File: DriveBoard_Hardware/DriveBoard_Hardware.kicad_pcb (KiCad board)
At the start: 2 copper layers, 20 parts, among them U1 MAX_3232, U2 MAX_3232, U3 OKI, U4 TM4C129E_Launchpad

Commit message: Made pcb layout
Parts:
- moved U1 93.7 mm to (136.1, 78.5)
- moved C7 91.1 mm to (161.7, 81.5)
- moved Conn2 88.0 mm to (131.3, 49.0)
- moved C3 87.9 mm to (129.7, 73.7)
- moved C4 84.3 mm to (129.7, 79.0)
- moved C8 81.7 mm to (161.7, 90.4)
- moved C9 80.9 mm to (145.8, 88.1)
- moved C11 80.6 mm to (158.9, 87.4)
- moved C2 80.0 mm to (126.1, 81.5)
- moved C1 77.9 mm to (126.1, 76.5)
- moved C12 76.7 mm to (142.4, 72.9)
- moved C10 74.7 mm to (145.9, 93.7)
- moved C5 73.4 mm to (142.2, 91.2)
- moved Conn3 70.5 mm to (148.6, 49.0)
- moved C6 68.0 mm to (142.1, 96.0)
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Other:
- board outline added: 61 x 99.8 mm

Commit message: Added PDR text files and made a few changes
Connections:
- net Net-(C7-Pad1) renamed /+12V
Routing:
- net +5V: track 0.00 -> 37.1 mm
- net /+12V: track 0.00 -> 26.6 mm

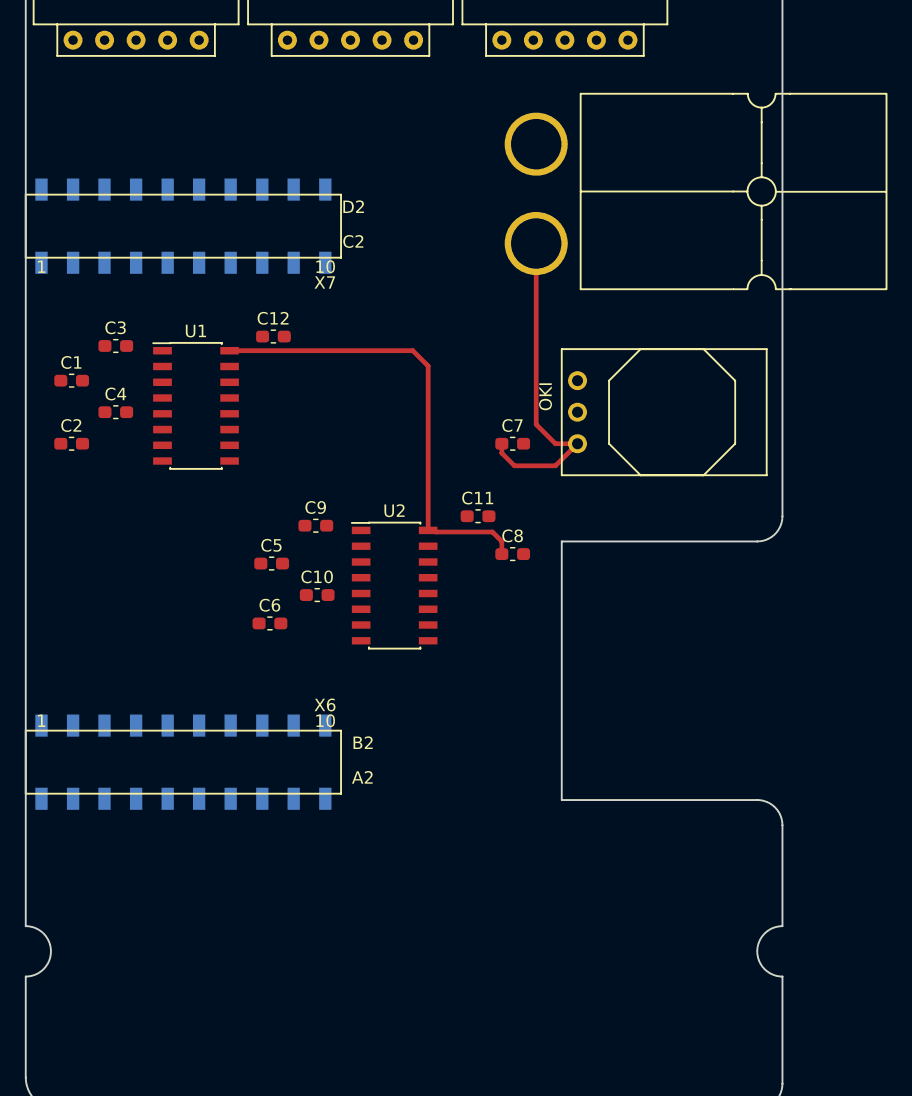
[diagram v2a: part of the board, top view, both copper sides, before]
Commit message: Updated silkscreens
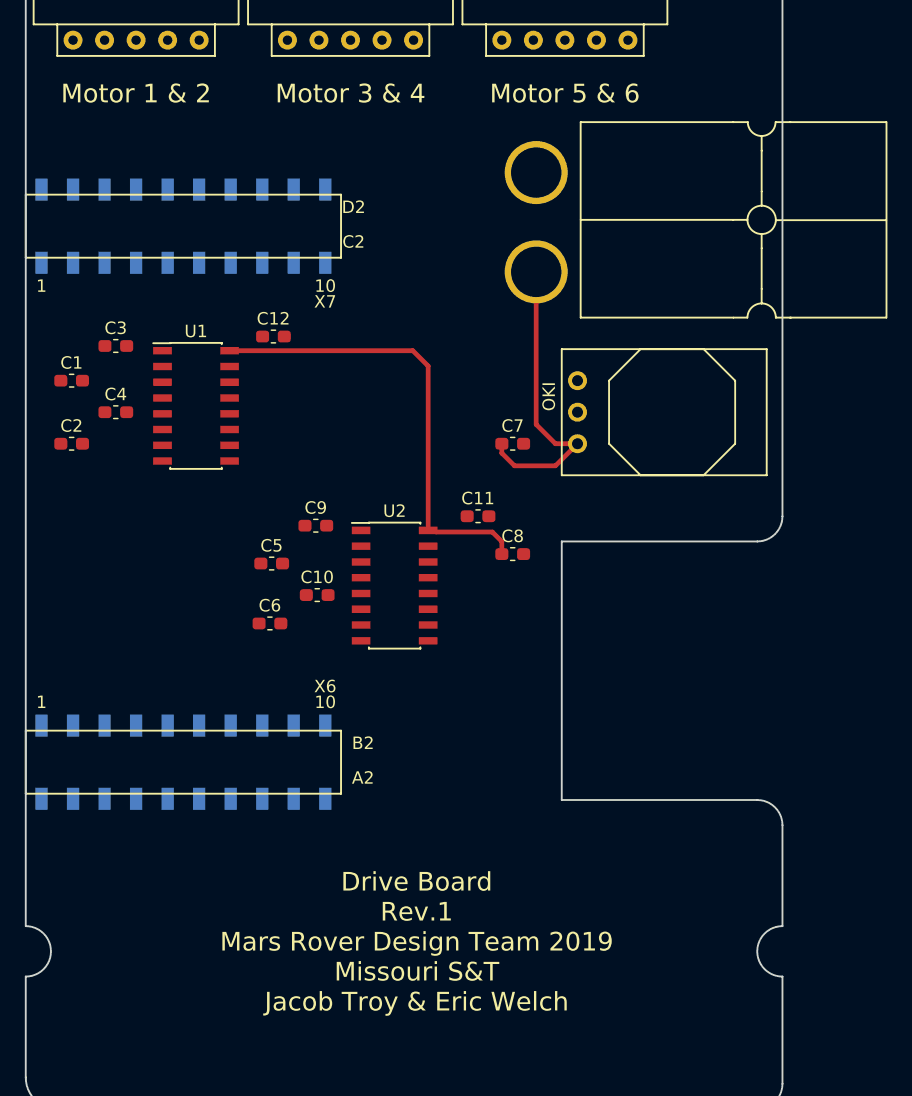
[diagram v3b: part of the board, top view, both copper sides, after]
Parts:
- moved Conn1 2.29 mm to (167.1, 55.6)
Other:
- board text added: "Drive Board Rev.1 Mars Rover Design Team 2019 Missouri S&T Jacob Troy & Eric Welch"
- board text added: "Motor 1 & 2"
- board text added: "Motor 3 & 4"
- board text added: "Motor 5 & 6"
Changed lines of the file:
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@@
   (general
     (thickness 1.6)
-    (drawings 17)
+    (drawings 21)
     (tracks 15)
     (zones 0)
@@
   )
   (module MRDT_Connectors:Anderson_2_Horisontal_Side_by_Side (layer F.Cu)
-    (at 167.132 53.34 180)
+    (at 167.132 55.626 180)
     (fp_text reference Conn1 (at -1.8796 0.762 180) (layer F.SilkS) hide
       (effects (font (size 1 1) (thickness 0.15)))
@@
       (effects (font (size 1 1) (thickness 0.15)))
     )
-    (fp_text value OKI (at 6.35 -1.27 90) (layer F.SilkS)
+    (fp_text value OKI (at 6.35 -1.016 90) (layer F.SilkS)
       (effects (font (size 1 1) (thickness 0.15)))
     )
@@
       (effects (font (size 1 1) (thickness 0.15)))
     )
-    (fp_text user 1 (at 1.27 -42.418 180) (layer F.SilkS)
-      (effects (font (size 1 1) (thickness 0.15)))
-    )
-    (fp_text user 10 (at 24.13 -42.418 180) (layer F.SilkS)
-      (effects (font (size 1 1) (thickness 0.15)))
-    )
-    (fp_text user 10 (at 24.13 -5.842 180) (layer F.SilkS)
-      (effects (font (size 1 1) (thickness 0.15)))
-    )
-    (fp_text user 1 (at 1.27 -5.842 180) (layer F.SilkS)
-      (effects (font (size 1 1) (thickness 0.15)))
-    )
-    (fp_text user X7 (at 24.13 -41.148 180) (layer F.SilkS)
-      (effects (font (size 1 1) (thickness 0.15)))
-    )
-    (fp_text user X6 (at 24.13 -7.112) (layer F.SilkS)
+    (fp_text user 1 (at 1.27 -40.894 180) (layer F.SilkS)
+      (effects (font (size 1 1) (thickness 0.15)))
+    )
+    (fp_text user 10 (at 24.13 -40.894 180) (layer F.SilkS)
+      (effects (font (size 1 1) (thickness 0.15)))
+    )
+    (fp_text user 10 (at 24.13 -7.366 180) (layer F.SilkS)
+      (effects (font (size 1 1) (thickness 0.15)))
+    )
+    (fp_text user 1 (at 1.27 -7.366 180) (layer F.SilkS)
+      (effects (font (size 1 1) (thickness 0.15)))
+    )
+    (fp_text user X7 (at 24.13 -39.624 180) (layer F.SilkS)
+      (effects (font (size 1 1) (thickness 0.15)))
+    )
+    (fp_text user X6 (at 24.13 -8.636) (layer F.SilkS)
       (effects (font (size 1 1) (thickness 0.15)))
     )
@@
       (net 67 "Net-(U4-PadPP5)"))
   )
+  (gr_text "Motor 5 & 6" (at 165.862 53.34) (layer F.SilkS)
+    (effects (font (size 1.5 1.5) (thickness 0.3)))
+  )
+  (gr_text "Motor 3 & 4" (at 148.59 53.34) (layer F.SilkS)
+    (effects (font (size 1.5 1.5) (thickness 0.3)))
+  )
+  (gr_text "Motor 1 & 2" (at 131.318 53.34) (layer F.SilkS)
+    (effects (font (size 1.5 1.5) (thickness 0.3)))
+  )
+  (gr_text "Drive Board\nRev.1\nMars Rover Design Team 2019\nMissouri S&T\nJacob Troy & Eric Welch" (at 153.924 121.666) (layer F.SilkS)
+    (effects (font (size 1.5 1.5) (thickness 0.3)))
+  )
   (gr_arc (start 181.356 87.376) (end 181.356 89.408) (angle -90) (layer Edge.Cuts) (width 0.15))

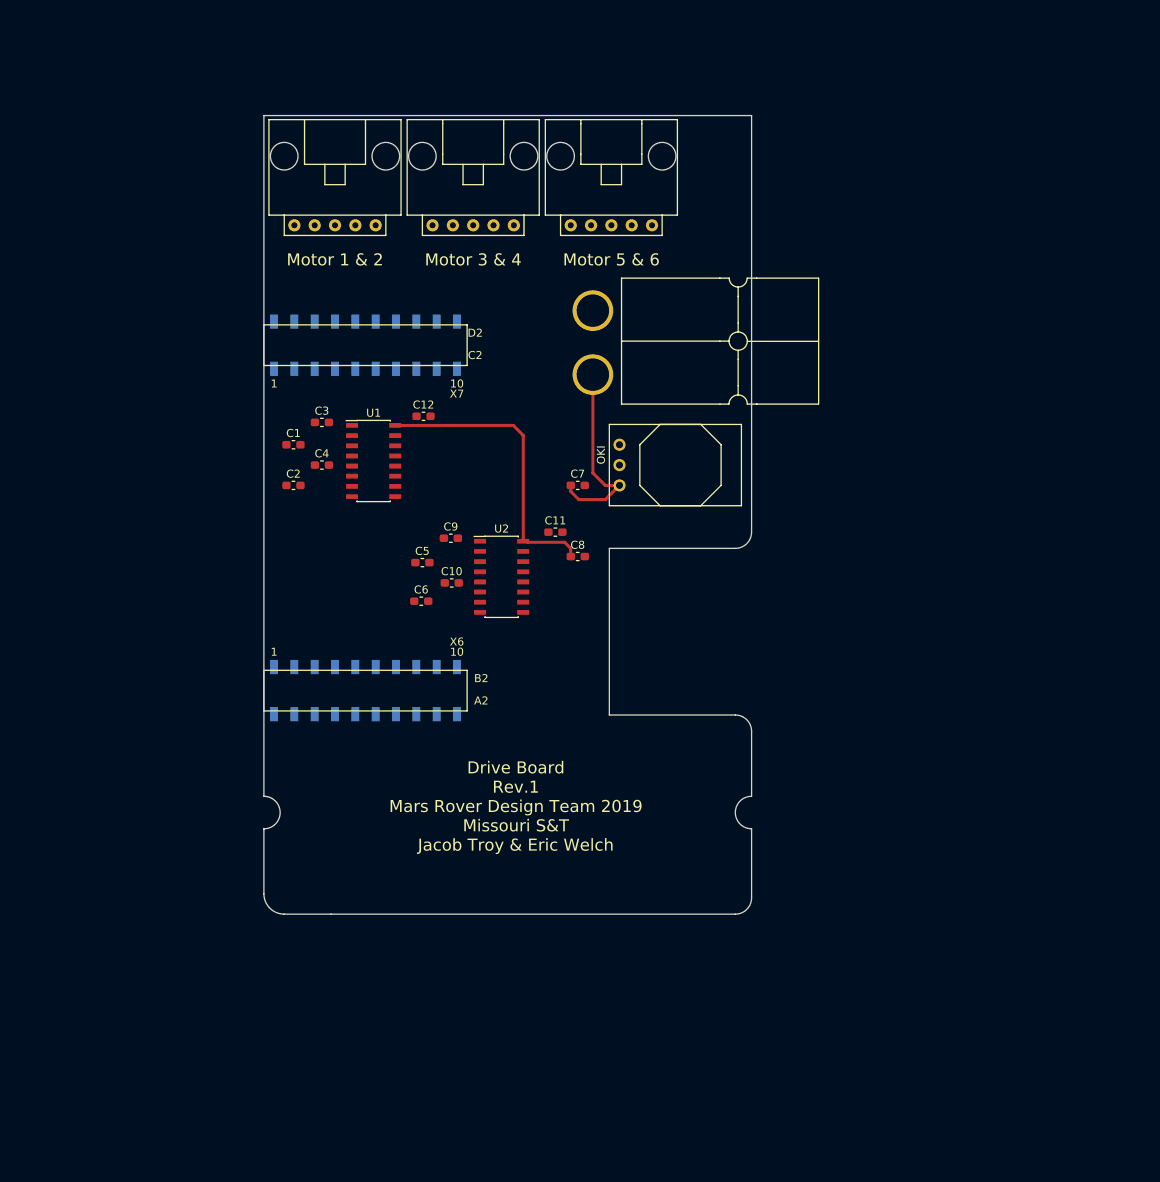
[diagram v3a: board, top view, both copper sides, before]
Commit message: Added traces to pcb layout
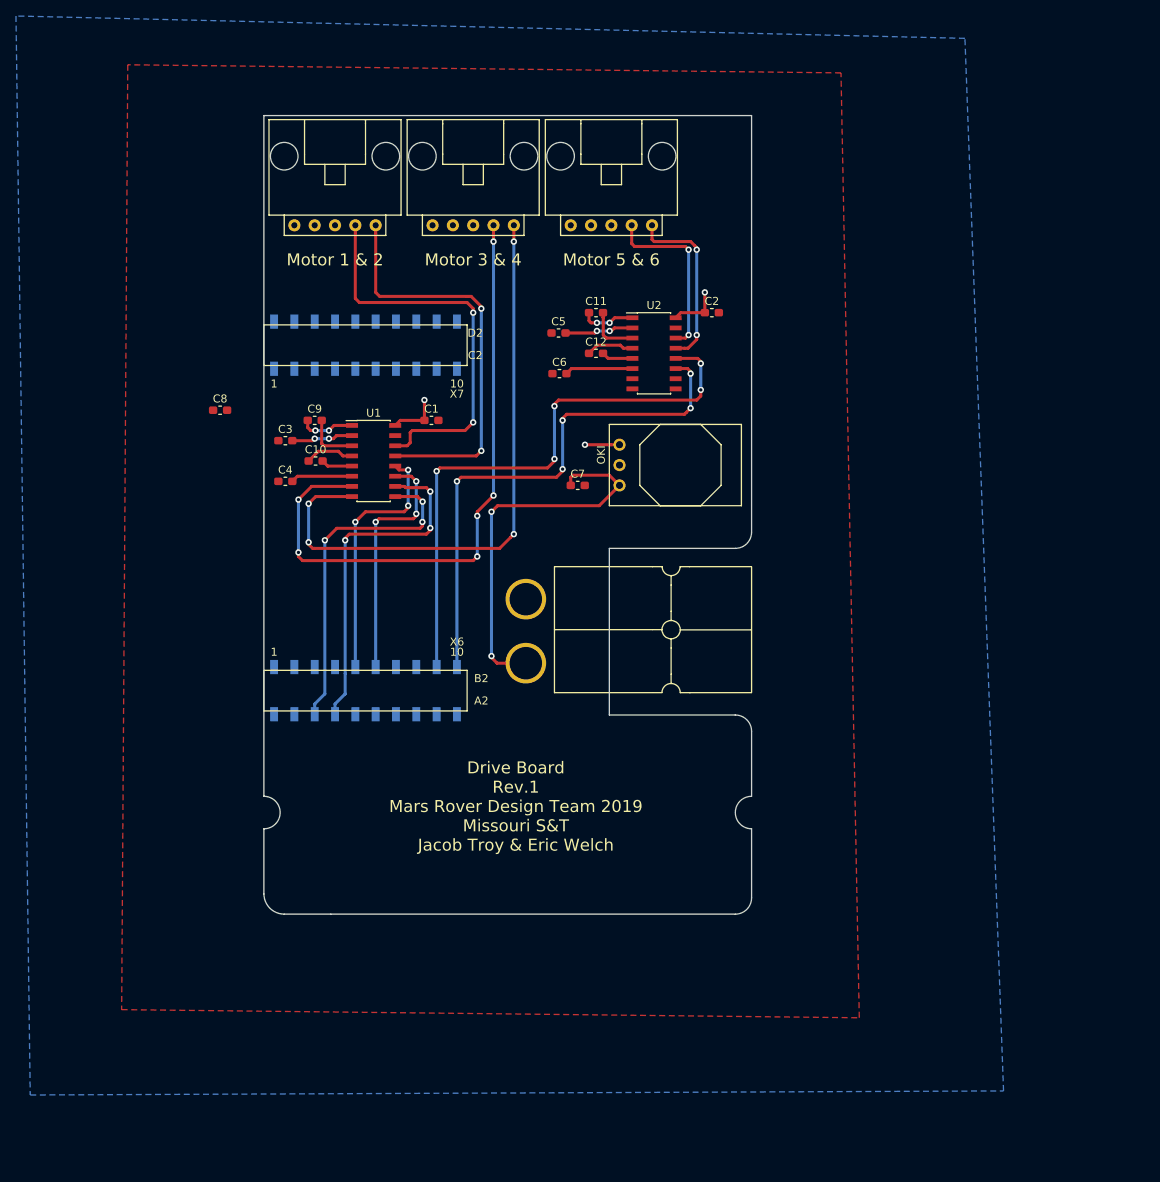
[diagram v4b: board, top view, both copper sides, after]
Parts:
- moved C2 56.6 mm to (178.4, 59.9)
- moved C8 48.3 mm to (117.0, 72.1)
- moved Conn1 37.0 mm to (158.8, 91.7)
- moved U2 33.8 mm to (171.2, 65.0)
- moved C5 33.4 mm to (159.3, 62.5)
- moved C6 33.3 mm to (159.4, 67.6)
- moved C11 27.9 mm to (163.9, 59.9)
- moved C12 23.0 mm to (163.9, 65.0)
- moved C10 22.8 mm to (128.9, 78.5)
- moved C9 22.5 mm to (128.8, 73.4)
- moved C1 17.5 mm to (143.4, 73.4)
- moved C3 5.11 mm to (125.1, 75.9)
- moved C4 5.00 mm to (125.1, 81.0)
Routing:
- net TX_2_SL: track 0.00 -> 79.5 mm, vias 0 -> 6
- net RX_2_SL: track 0.00 -> 76.1 mm, vias 0 -> 4
- net RX_3_IC: track 0.00 -> 73.2 mm, vias 0 -> 5
- net TX_3_IC: track 0.00 -> 66.7 mm, vias 0 -> 5
- net RX_1_SL: track 0.00 -> 51.4 mm, vias 0 -> 2
- net TX_1_SL: track 0.00 -> 50.3 mm, vias 0 -> 2
- net TX_2_IC: track 0.00 -> 43.1 mm, vias 0 -> 3
- net RX_2_IC: track 0.00 -> 41.9 mm, vias 0 -> 3
- net RX_1_IC: track 0.00 -> 32.0 mm, vias 0 -> 3
- net TX_1_IC: track 0.00 -> 30.7 mm, vias 0 -> 3
- net RX_3_SL: track 0.00 -> 22.4 mm, vias 0 -> 2
- net TX_3_SL: track 0.00 -> 22.2 mm, vias 0 -> 2
- net /+12V: track 26.6 -> 47.9 mm, vias 0 -> 2
- net +5V: track 37.1 -> 17.9 mm, vias 0 -> 3
- net Net-(C5-Pad2): track 0.00 -> 8.63 mm, vias 0 -> 2
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- added copper zone on B.Cu, net +5V
- added copper zone on F.Cu, net GND

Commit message: Updated some connections
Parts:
- moved C8 46.1 mm to (162.4, 80.0)
- moved C7 5.95 mm to (159.6, 87.1)
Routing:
- net +5V: track 17.9 -> 23.2 mm
- net /+12V: track 47.9 -> 43.2 mm
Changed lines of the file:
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@@
     (thickness 1.6)
     (drawings 21)
-    (tracks 260)
+    (tracks 264)
     (zones 0)
     (modules 20)
@@
   )
   (module Capacitor_SMD:C_0603_1608Metric_Pad1.05x0.95mm_HandSolder (layer F.Cu)
-    (at 161.657 81.534)
+    (at 159.625 87.122)
     (descr "Capacitor SMD 0603 (1608 Metric), square (rectangular) end terminal, IPC_7351 nominal with elongated pad for handsoldering. (Body size source: http://www.tortai-tech.com/upload/download/2011102023233369053.pdf), generated with kicad-footprint-generator")
     (tags "capacitor handsolder")
@@
   )
   (module Capacitor_SMD:C_0603_1608Metric_Pad1.05x0.95mm_HandSolder (layer F.Cu)
-    (at 116.953 72.136)
+    (at 162.419 80.01)
     (descr "Capacitor SMD 0603 (1608 Metric), square (rectangular) end terminal, IPC_7351 nominal with elongated pad for handsoldering. (Body size source: http://www.tortai-tech.com/upload/download/2011102023233369053.pdf), generated with kicad-footprint-generator")
     (tags "capacitor handsolder")
@@
   (segment (start 173.896 60.579) (end 174.346 60.579) (width 0.25) (layer F.Cu) (net 2))
   (via (at 162.56 76.454) (size 0.8) (drill 0.4) (layers F.Cu B.Cu) (net 2))
-  (segment (start 165.80037 76.454) (end 162.56 76.454) (width 0.381) (layer F.Cu) (net 2))
   (segment (start 166.878 76.454) (end 165.80037 76.454) (width 0.381) (layer F.Cu) (net 2))
   (segment (start 174.531 59.944) (end 173.896 60.579) (width 0.381) (layer F.Cu) (net 2))
@@
   (via (at 177.546 57.404) (size 0.8) (drill 0.4) (layers F.Cu B.Cu) (net 2))
   (segment (start 177.546 59.944) (end 177.546 57.404) (width 0.381) (layer F.Cu) (net 2))
+  (segment (start 163.83 76.454) (end 162.56 76.454) (width 0.381) (layer F.Cu) (net 2))
+  (segment (start 165.80037 76.454) (end 163.83 76.454) (width 0.381) (layer F.Cu) (net 2))
+  (segment (start 161.544 80.01) (end 161.544 78.994) (width 0.381) (layer F.Cu) (net 2))
+  (segment (start 161.544 78.994) (end 162.052 78.486) (width 0.381) (layer F.Cu) (net 2))
+  (segment (start 162.052 78.486) (end 163.576 78.486) (width 0.381) (layer F.Cu) (net 2))
+  (segment (start 163.83 78.232) (end 163.83 76.454) (width 0.381) (layer F.Cu) (net 2))
+  (segment (start 163.576 78.486) (end 163.83 78.232) (width 0.381) (layer F.Cu) (net 2))
   (via (at 128.778 75.692) (size 0.8) (drill 0.4) (layers F.Cu B.Cu) (net 3))
   (segment (start 125.984 75.946) (end 128.524 75.946) (width 0.381) (layer F.Cu) (net 3))
@@
   (segment (start 177.038 69.596) (end 177.038 70.358) (width 0.381) (layer F.Cu) (net 36))
   (segment (start 177.038 70.358) (end 176.53 70.866) (width 0.381) (layer F.Cu) (net 36))
-  (segment (start 165.608 80.264) (end 166.878 81.534) (width 0.381) (layer F.Cu) (net 68))
-  (segment (start 161.036 80.264) (end 165.608 80.264) (width 0.381) (layer F.Cu) (net 68))
-  (segment (start 160.782 81.534) (end 160.782 80.518) (width 0.381) (layer F.Cu) (net 68))
-  (segment (start 160.782 80.518) (end 161.036 80.264) (width 0.381) (layer F.Cu) (net 68))
   (segment (start 151.576498 103.758) (end 150.876 103.057502) (width 0.381) (layer F.Cu) (net 68))
   (segment (start 155.1686 103.758) (end 151.576498 103.758) (width 0.381) (layer F.Cu) (net 68))
@@
   (segment (start 164.338 84.074) (end 166.878 81.534) (width 0.381) (layer F.Cu) (net 68))
   (segment (start 150.876 84.836) (end 151.638 84.074) (width 0.381) (layer F.Cu) (net 68))
-  (segment (start 151.638 84.074) (end 164.338 84.074) (width 0.381) (layer F.Cu) (net 68))
+  (segment (start 158.75 84.074) (end 164.338 84.074) (width 0.381) (layer F.Cu) (net 68))
+  (segment (start 151.638 84.074) (end 158.75 84.074) (width 0.381) (layer F.Cu) (net 68))
+  (segment (start 158.75 87.122) (end 158.75 84.074) (width 0.381) (layer F.Cu) (net 68))
   (zone (net 1) (net_name GND) (layer F.Cu) (hatch edge 0.508)
-    (connect_pads (clearance 0.508))
+    (connect_pads yes (clearance 0.508))
     (min_thickness 0.254)
     (fill yes (arc_segments 16) (thermal_gap 0.508) (thermal_bridge_width 0.508))
